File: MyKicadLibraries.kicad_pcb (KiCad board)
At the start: 2 copper layers, 168.6 x 118 mm, 35 parts, among them J1 Conn_01x08, J10 RCJ-22, J11 DIN-5, J12 Mini-DIN-6, J13 USB_A, J14 Conn_01x02, J15 Conn_01x02, J2 Conn_01x08, J3 POGO Pins, J4 c8-inlet, J5 FTDI, J6 Micro_SD_Card, J7 Conn_01x04, J8 Conn_02x04_Counter_Clockwise, J9 Conn_01x04, SW1 Schurter Switch, U1 radio-receiver, U10 rdm-6300, U11 magnetic-charger, U12 adafruit-MAX98357, U13 TTL, U14 lxb18, U15 esp32-wemos-d1-mini, U16 TCRT5000, U17 opb607a, U2 TP4056, U3 LilygoSIMT7000G, U4 esp-01m, U5 relais_module, U6 ESP-01, U7 dcdc, U8 mems-mic, U9 ESP-12E

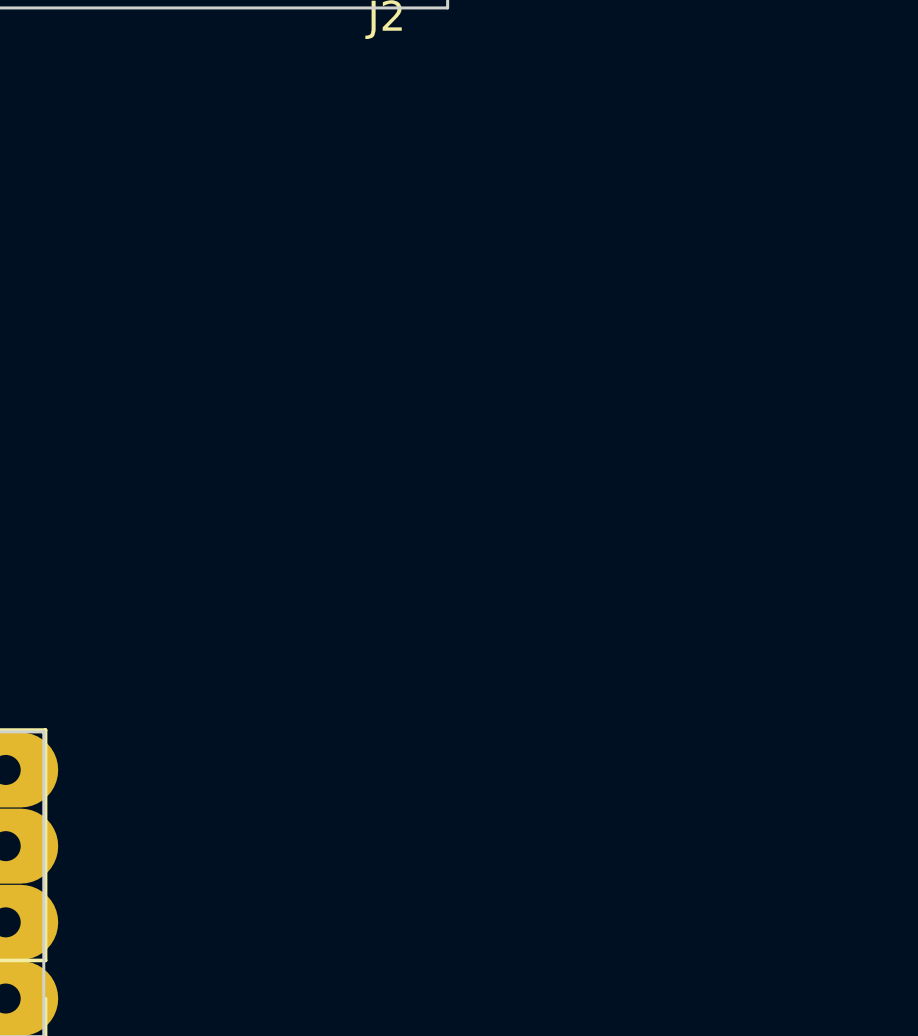
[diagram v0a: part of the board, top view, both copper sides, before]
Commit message: Add MAX98367 footprint
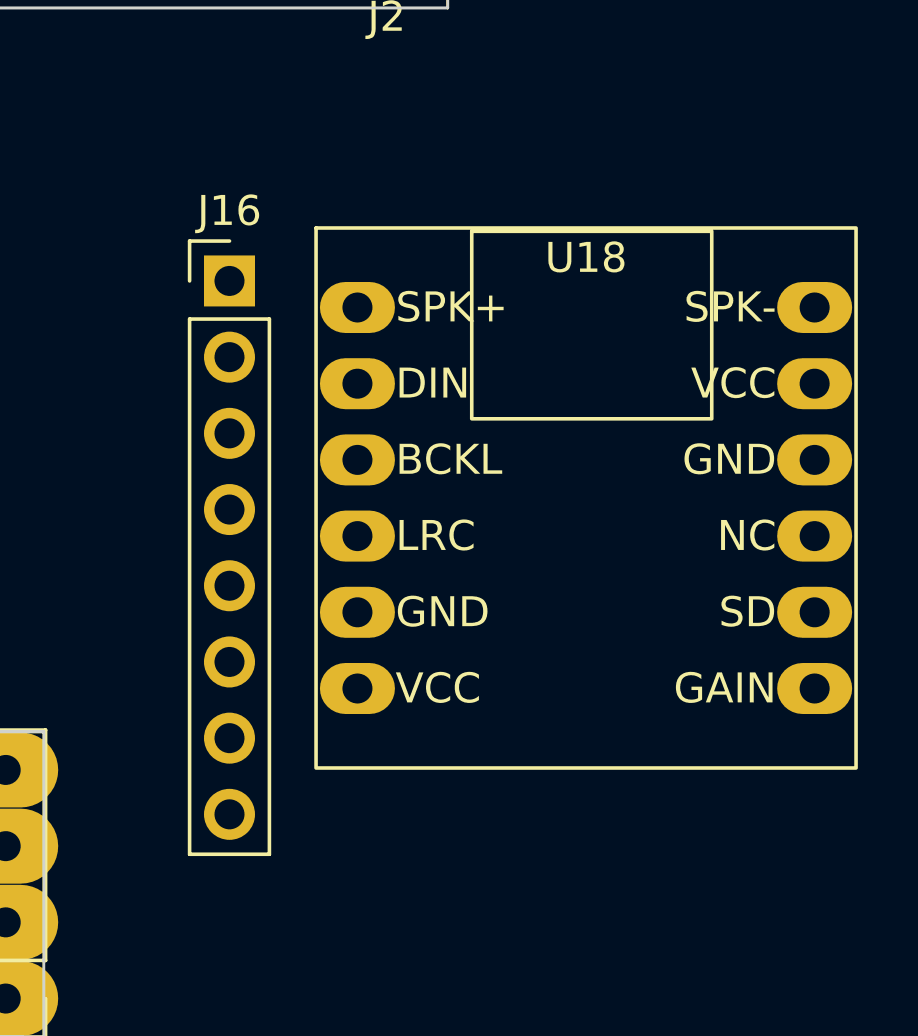
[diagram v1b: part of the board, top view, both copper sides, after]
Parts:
- added J16: Conn_01x08, Connector_PinHeader_2.54mm:PinHeader_1x08_P2.54mm_Vertical, F.Cu at (264.0, 98.0)
- added U18: max98367, max98367:max98367, F.Cu at (275.9, 105.2)
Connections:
- U4 pad 1: GND -> unconnected-(U4-Pad1)

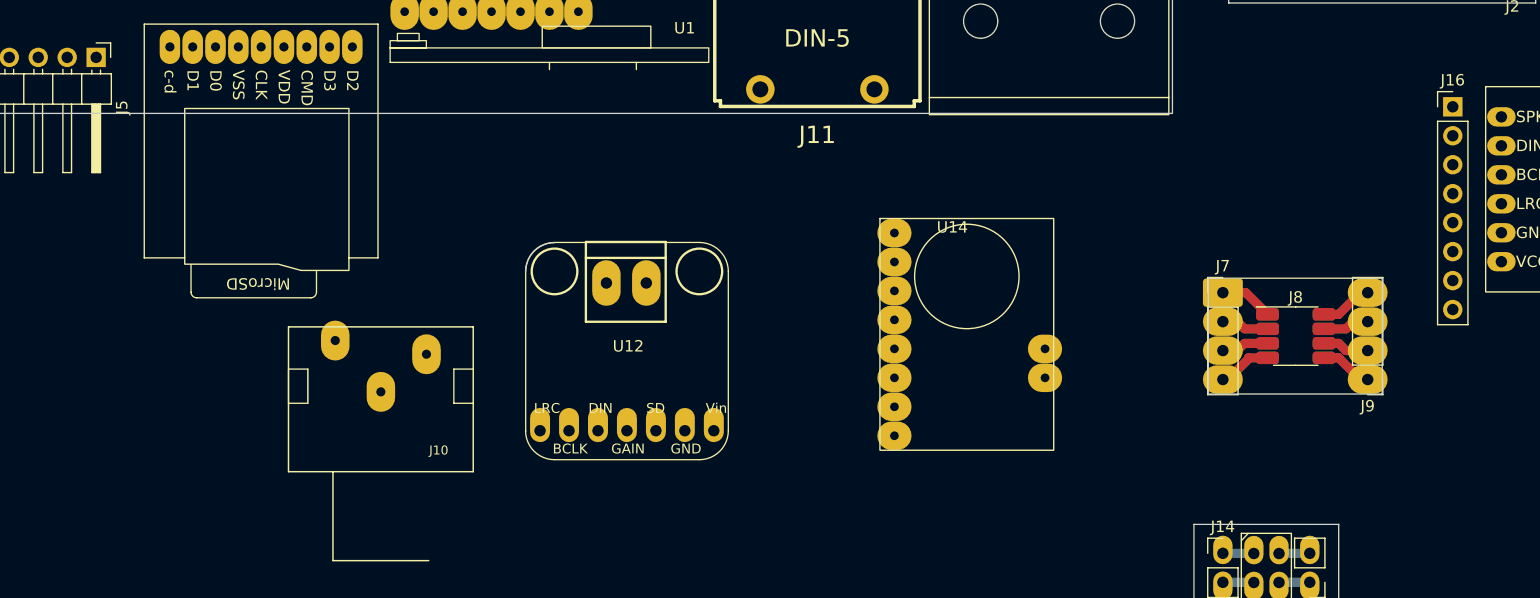
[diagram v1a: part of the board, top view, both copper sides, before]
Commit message: Add ESP-01F footprint
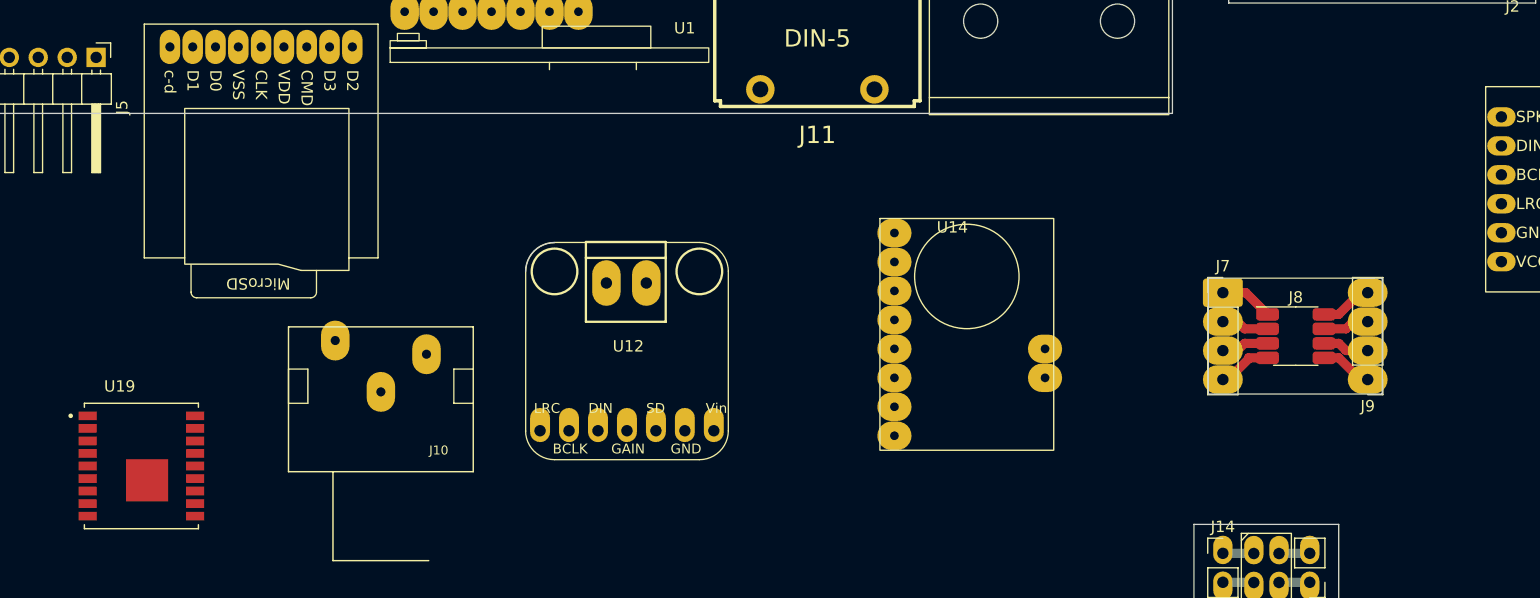
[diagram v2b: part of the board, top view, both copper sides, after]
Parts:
- removed J16: Conn_01x08, Connector_PinHeader_2.54mm:PinHeader_1x08_P2.54mm_Vertical
- added U19: MODULE_ESP-01F, esp-01f:esp-01f, F.Cu at (149.0, 129.5)
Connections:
- U18 pad 1: (no net) -> unconnected-(U18-Pad1)
- U18 pad 2: (no net) -> unconnected-(U18-Pad2)
- U18 pad 3: (no net) -> unconnected-(U18-Pad3)
- U18 pad 4: (no net) -> unconnected-(U18-Pad4)
- U18 pad 5: (no net) -> unconnected-(U18-Pad5)
- U18 pad 6: (no net) -> unconnected-(U18-Pad6)
- U18 pad 7: (no net) -> unconnected-(U18-Pad7)
- U18 pad 8: (no net) -> unconnected-(U18-Pad8)

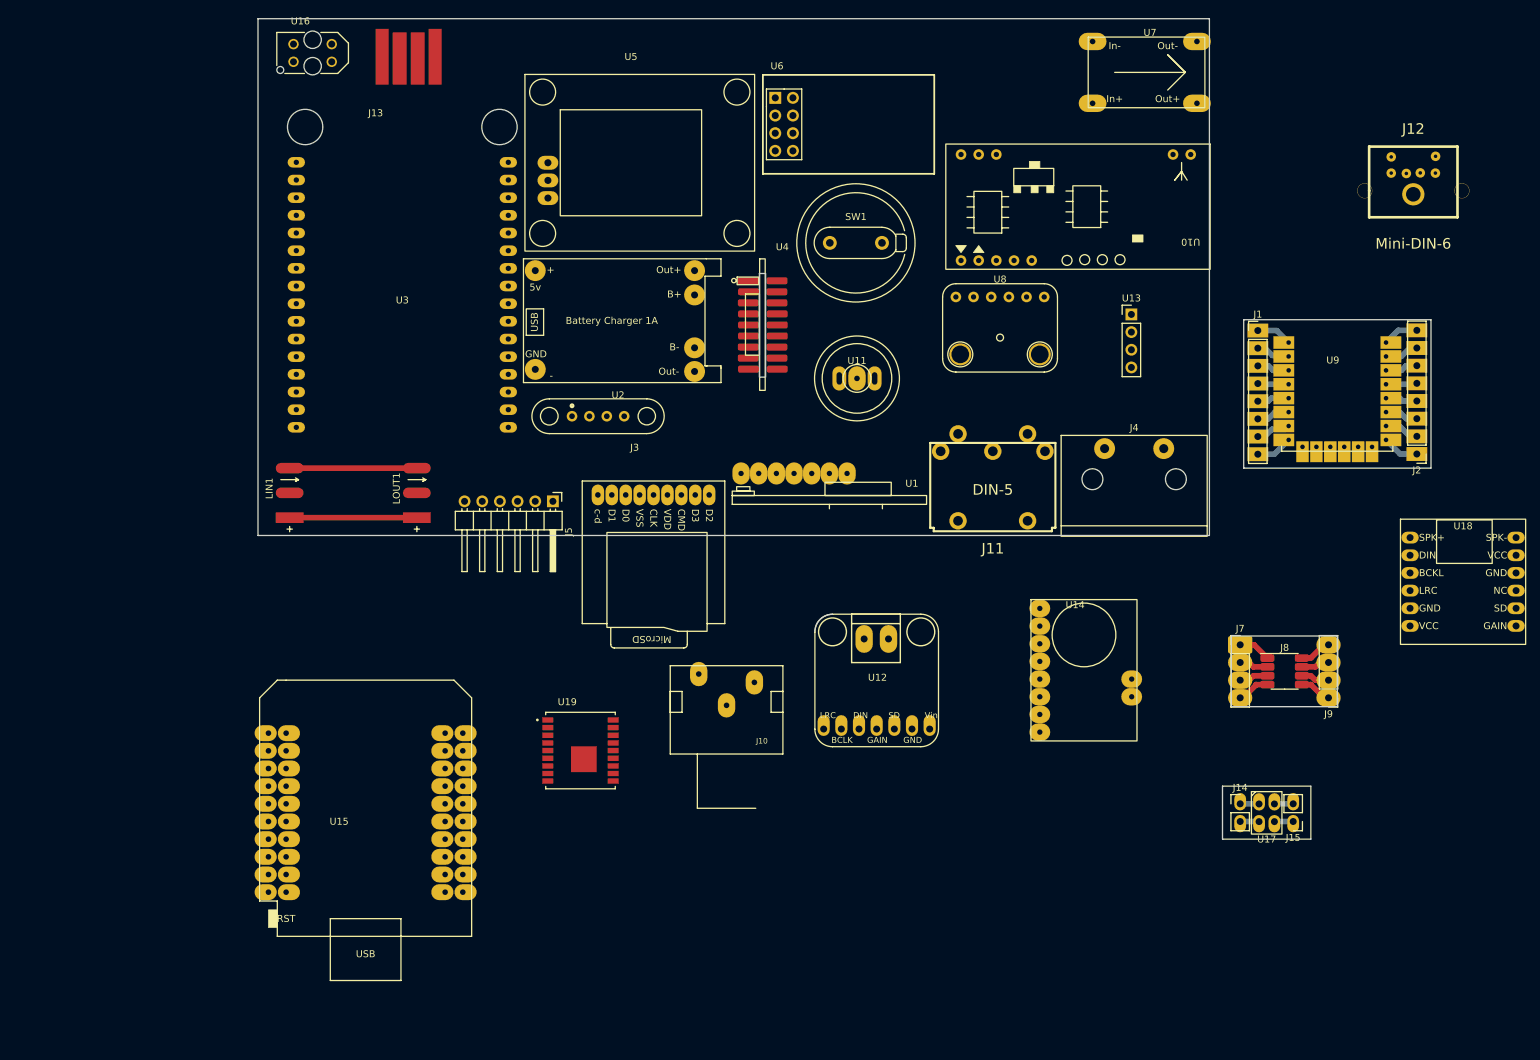
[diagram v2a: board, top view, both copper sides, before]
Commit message: Update tp4056 and fix edge cut issues
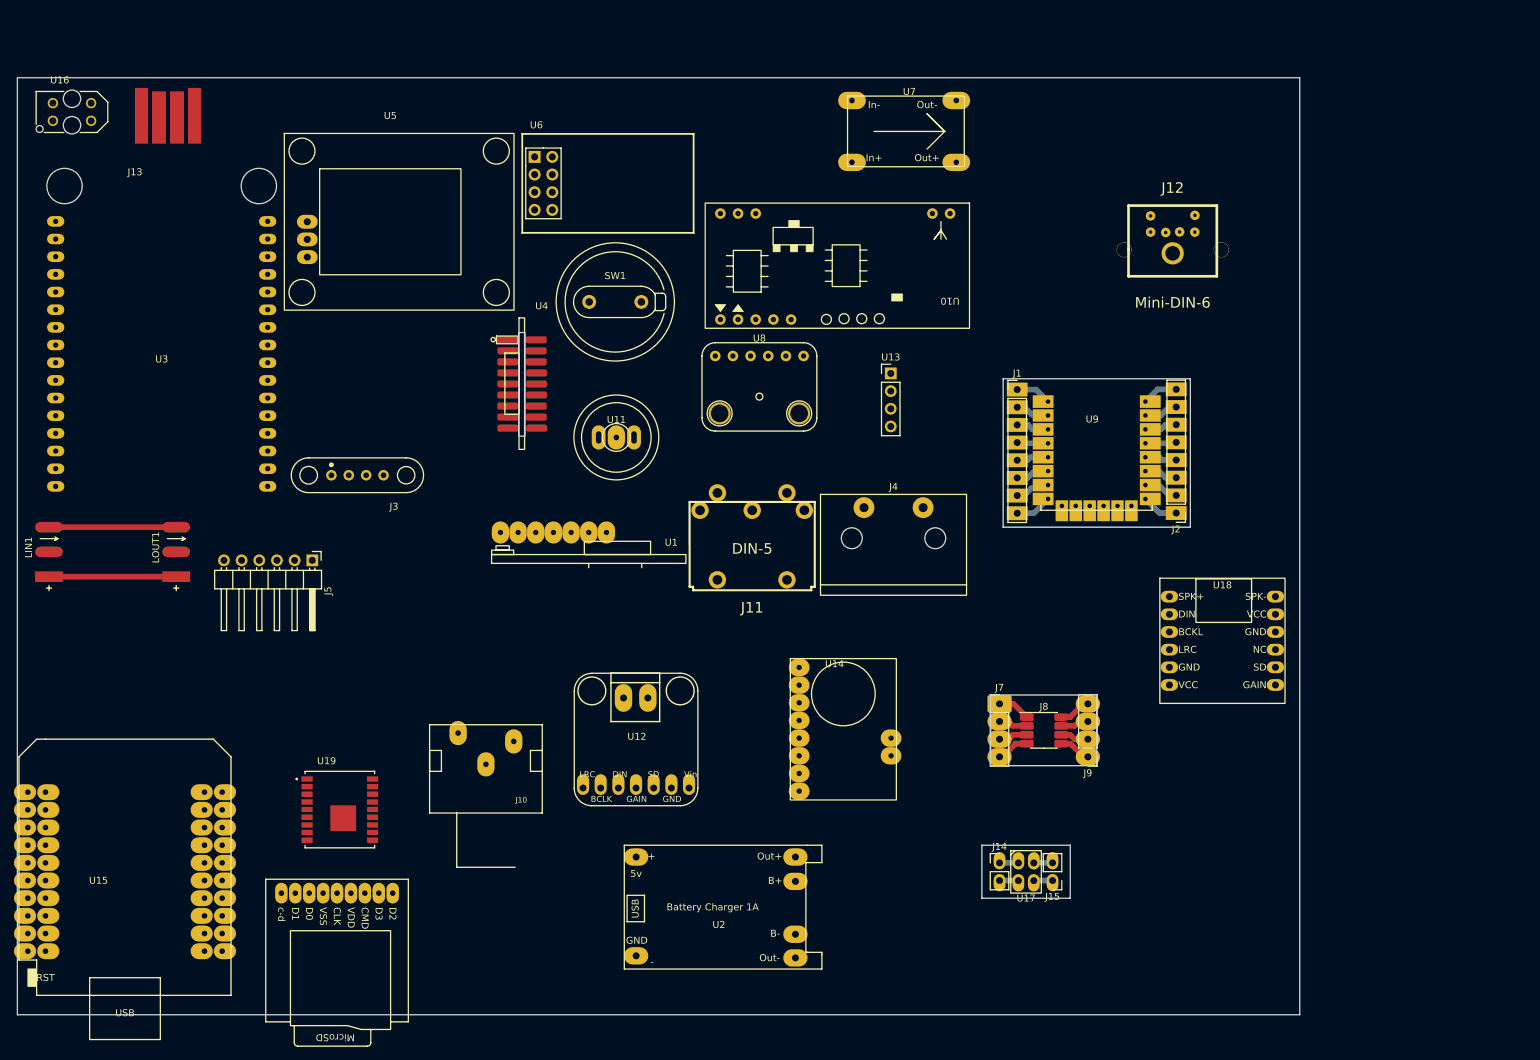
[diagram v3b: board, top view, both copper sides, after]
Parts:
- U19: value MODULE_ESP-01F -> esp-01f
- U2: value TP4056 -> tp4056; footprint TP4056:TP4056 -> tp4056:tp4056
- moved U2 97.1 mm to (168.0, 152.0)
- moved J6 73.1 mm to (114.0, 150.0)
- moved J12 35.6 mm to (234.1, 56.2)
- moved J9 35.6 mm to (221.9, 130.4)
- moved J10 35.6 mm to (135.4, 128.5)
- moved J14 35.6 mm to (209.2, 145.6)
- moved J15 35.6 mm to (216.9, 148.2)
- moved U17 35.6 mm to (213.1, 146.9)
- moved U19 35.6 mm to (114.4, 138.0)
- moved J1 35.6 mm to (211.8, 77.6)
- moved J11 35.6 mm to (173.7, 98.0)
- moved J13 35.6 mm to (83.7, 45.3)
- moved J2 35.6 mm to (234.6, 95.4)
- moved J3 35.6 mm to (116.9, 89.9)
- moved J4 35.6 mm to (194.0, 94.6)
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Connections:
- U2 pad 6: Net-(BT1-Pad2) -> unconnected-(U2-Pad6)
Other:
- board size 168.6 x 118 mm -> 184.4 x 134.7 mm
